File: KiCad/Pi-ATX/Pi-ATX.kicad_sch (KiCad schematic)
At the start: 0 parts

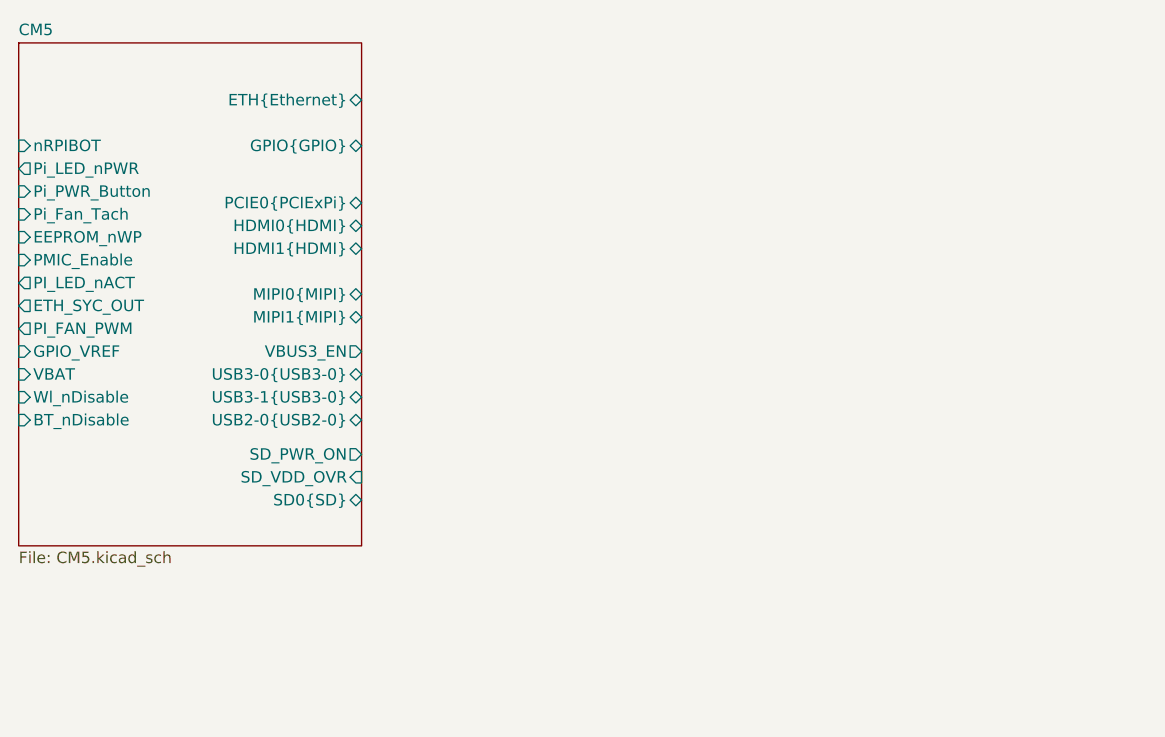
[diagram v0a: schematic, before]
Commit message: started mipi connectors
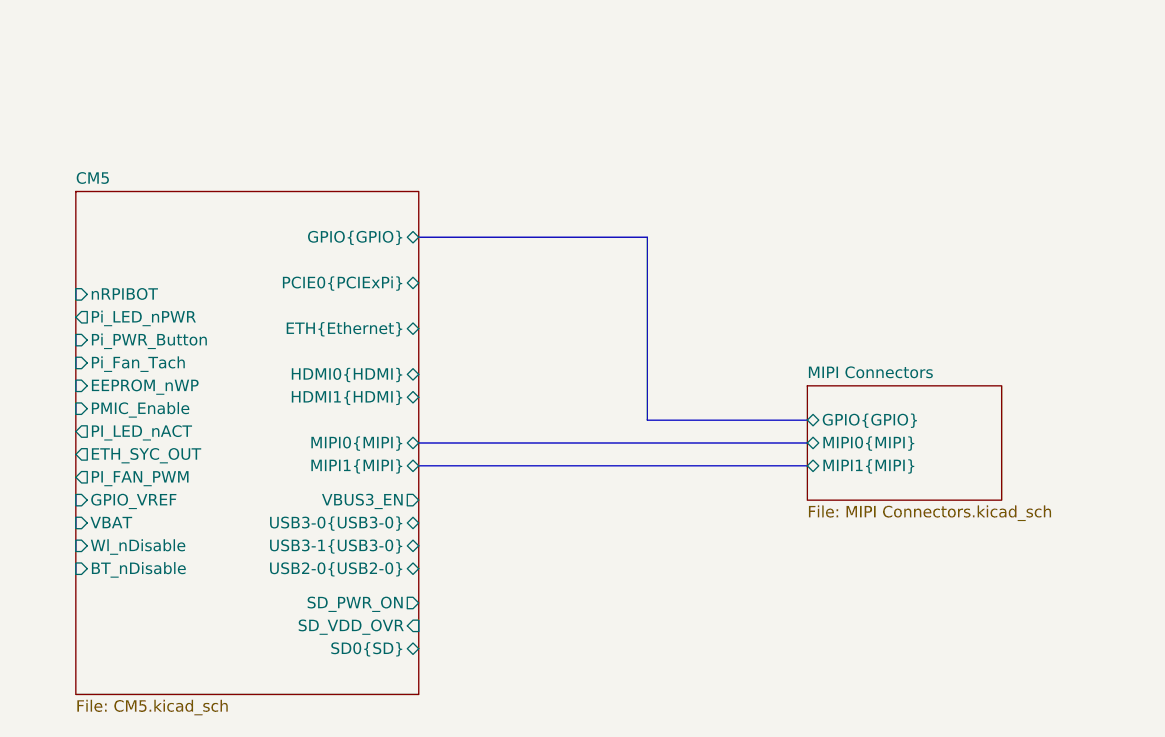
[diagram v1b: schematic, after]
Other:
- added sheet MIPI Connectors (MIPI Connectors.kicad_sch)

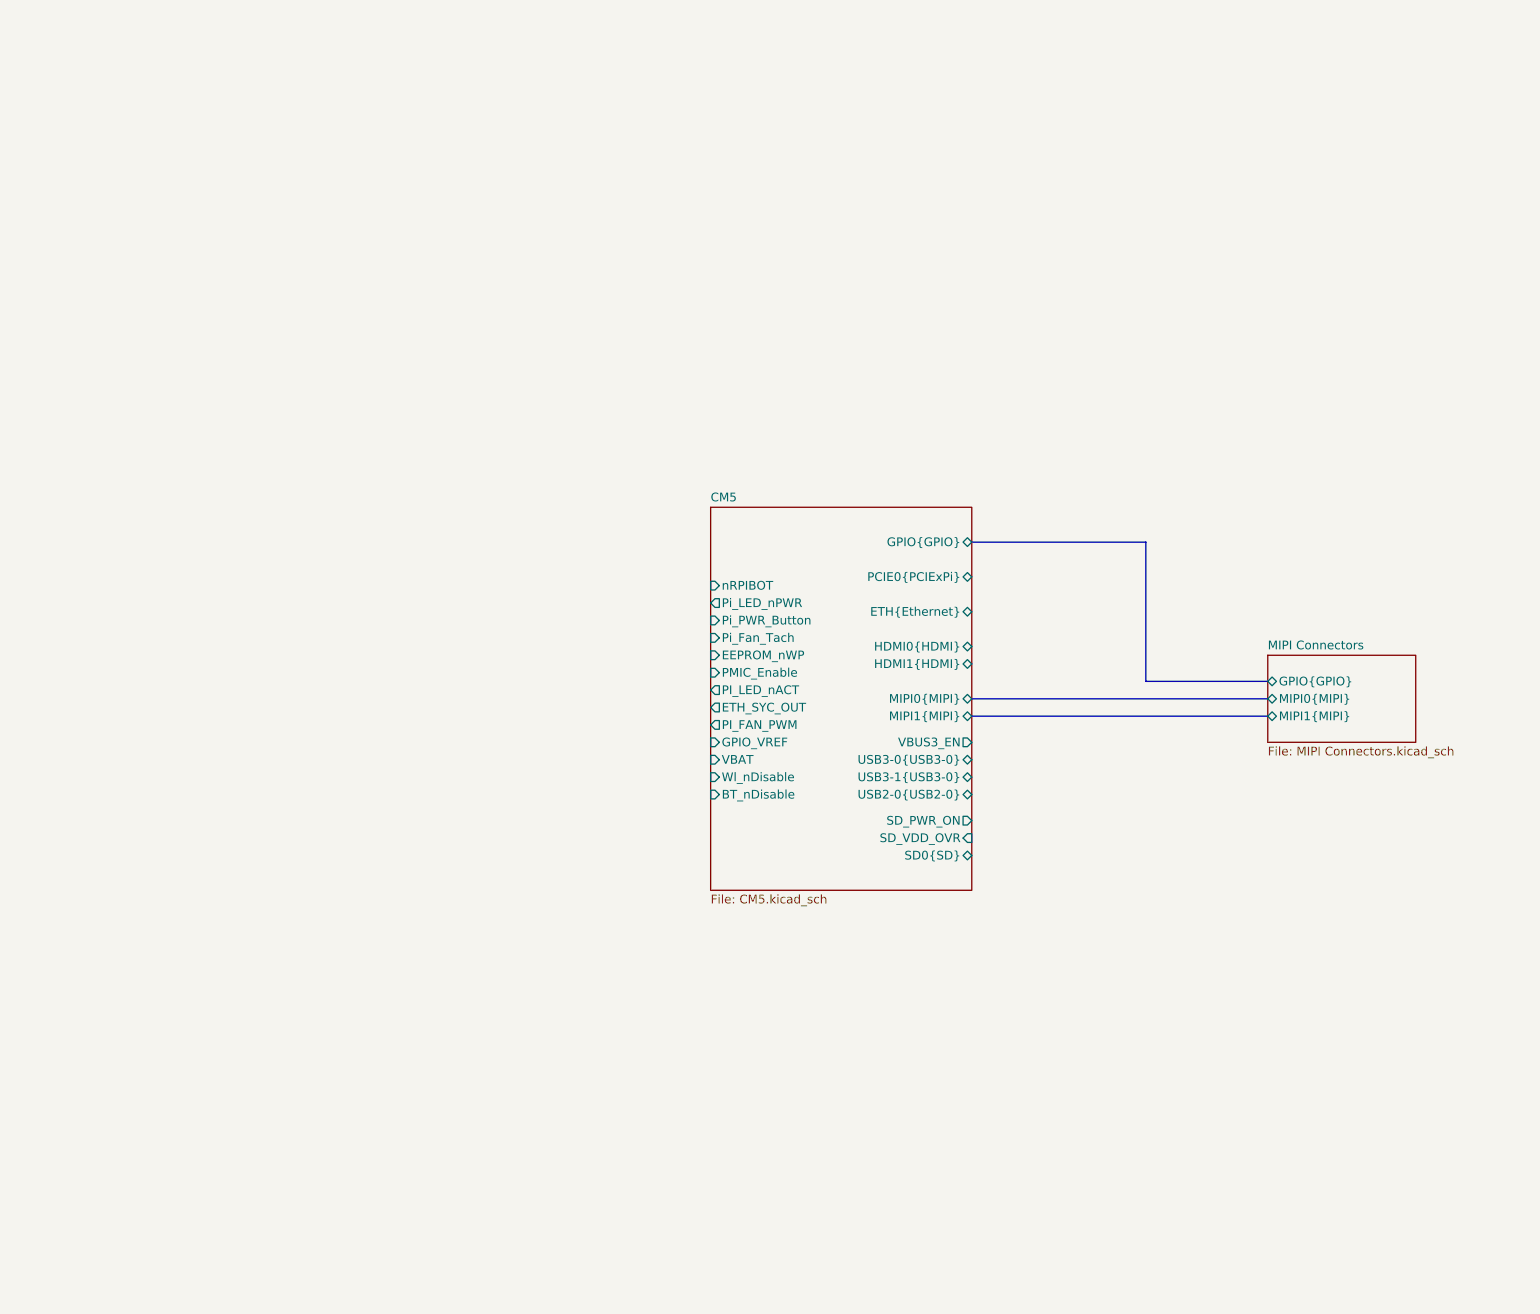
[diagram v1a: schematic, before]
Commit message: Finished MIPI Connector Schematic
-finished MIPI connector schematic page
-updated CM5 symbol to v0.2 version from my RPI CM library
-updated to do list
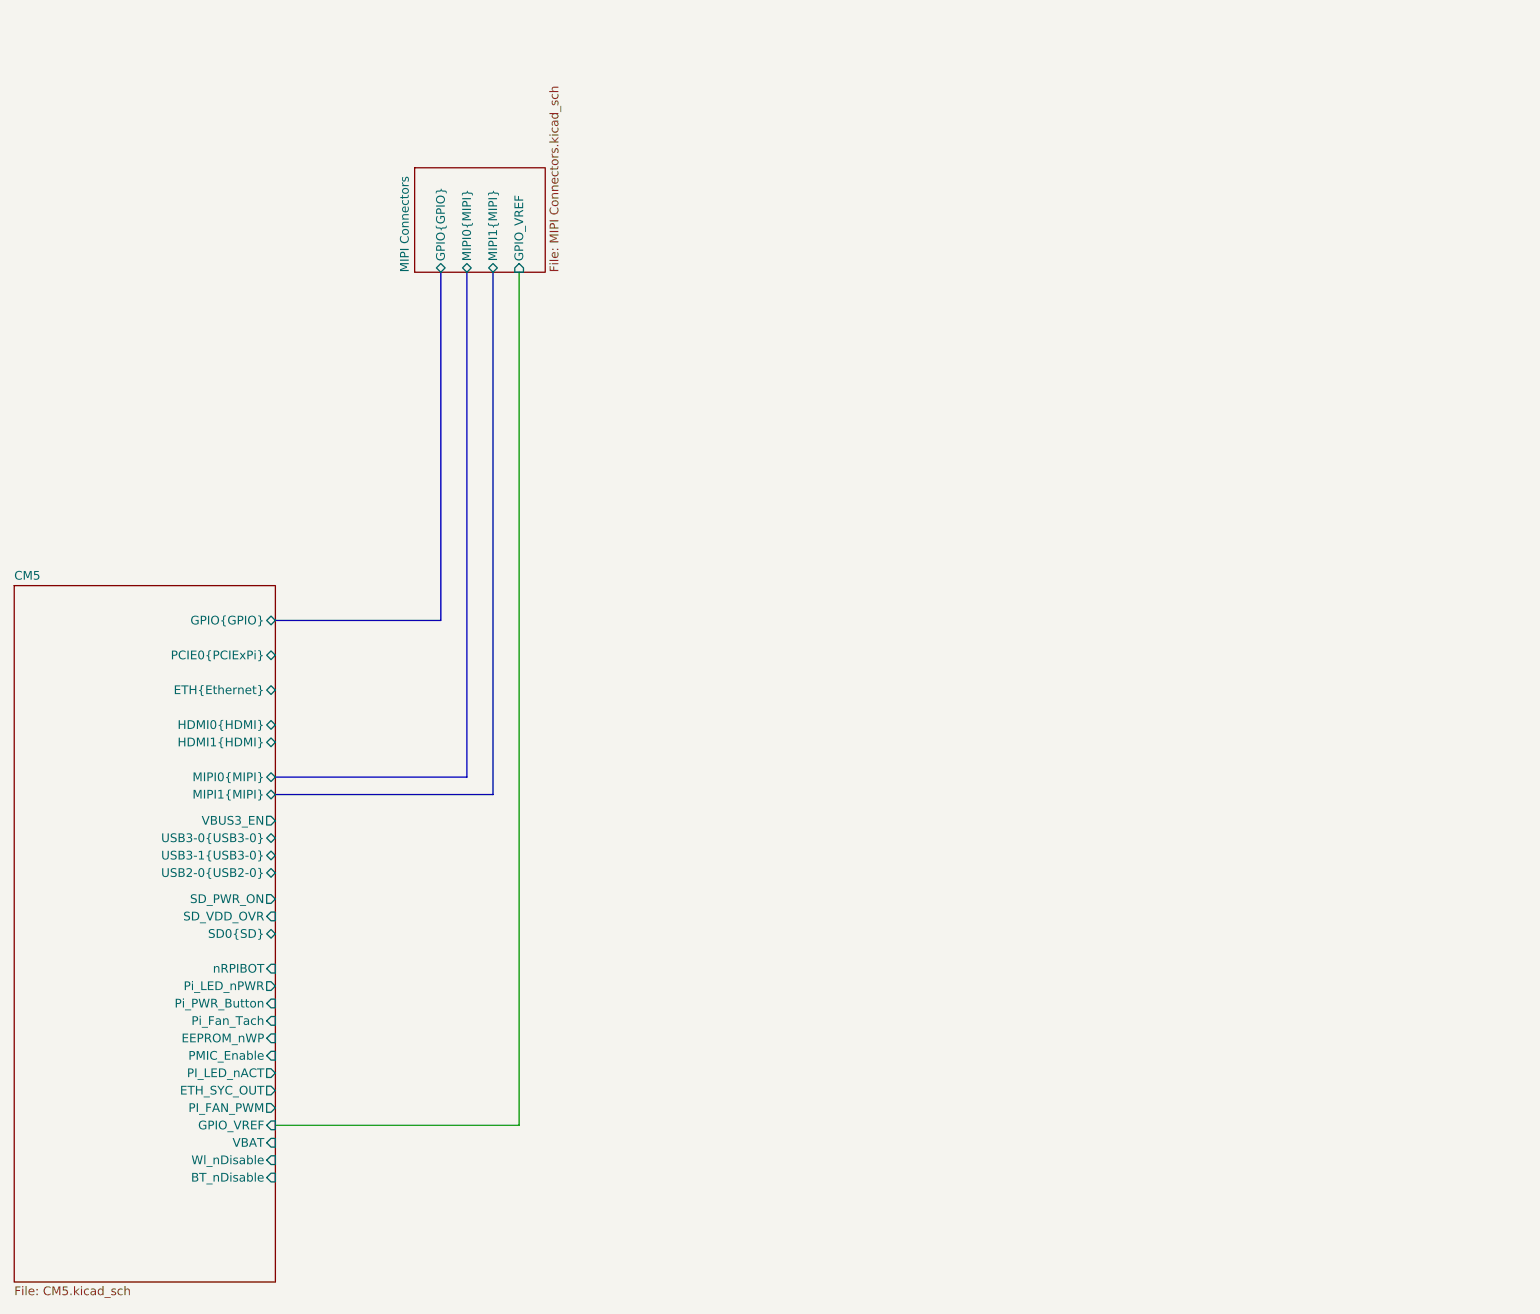
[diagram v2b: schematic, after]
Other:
- sheet MIPI Connectors ports: added GPIO_VREF; removed none
